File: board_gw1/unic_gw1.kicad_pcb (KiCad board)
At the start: 4 copper layers, 49.5 x 15.2 mm, 112 parts, among them Q1 2N7002, Q10 2N7002, Q11 2N7002, Q12 2N7002, Q13 2N7002, Q14 2N7002, Q15 2N7002, Q16 2N7002, Q17 2N7002, Q18 2N7002, Q19 2N7002, Q2 2N7002, Q20 2N7002, Q21 2N7002, Q22 2N7002, Q23 2N7002, Q24 2N7002, Q25 2N7002, Q26 2N7002, Q27 2N7002, Q28 2N7002, Q29 2N7002, Q3 2N7002, Q30 2N7002, Q31 2N7002, Q32 2N7002, Q33 2N7002, Q34 2N7002, Q35 2N7002, Q36 2N7002, Q37 2N7002, Q38 2N7002, Q39 2N7002, Q4 2N7002, Q40 2N7002, Q5 2N7002, Q6 2N7002, Q7 2N7002, Q8 2N7002, Q9 2N7002, U1 GW1N-LV9QN88C6_I5_, U2 LM3480-3.3, U3 AP2202K-ADJ, U4 APS6404L-3SQR-ZR, U6 AP62150Z6, U7 W25Q16JVUXIQ, X1 27MHz

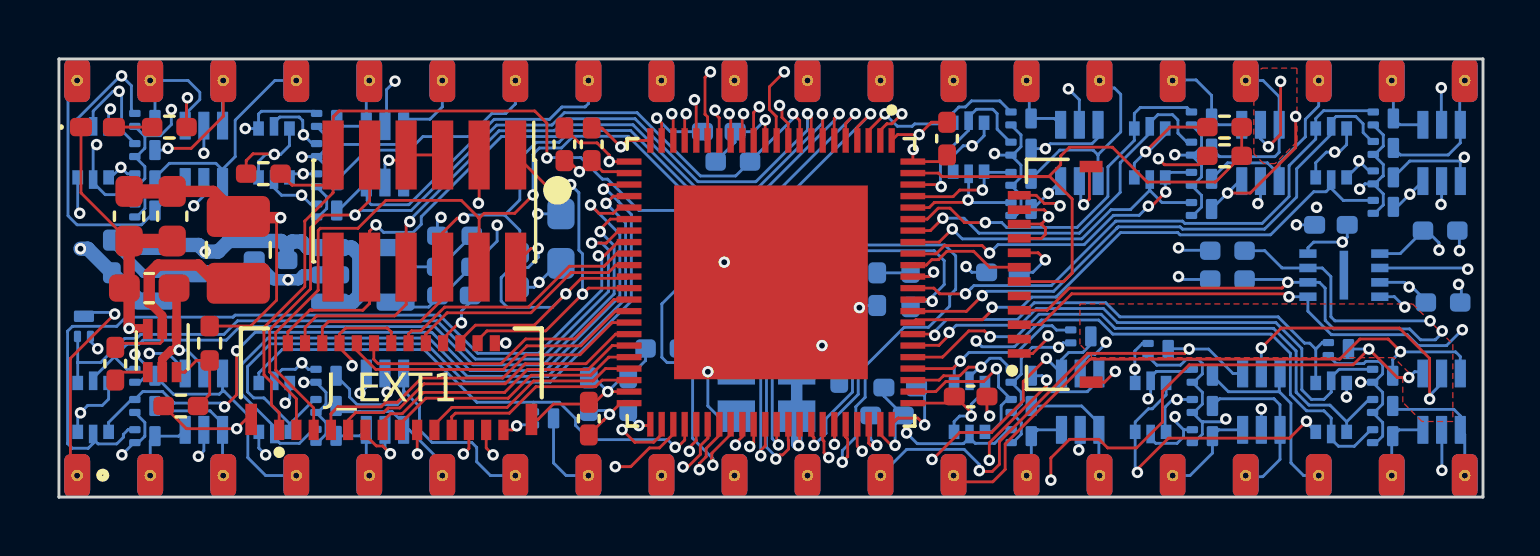
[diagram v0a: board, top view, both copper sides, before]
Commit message: Switched back to 0805 caps: they're cheaper. TODO: part number updates.
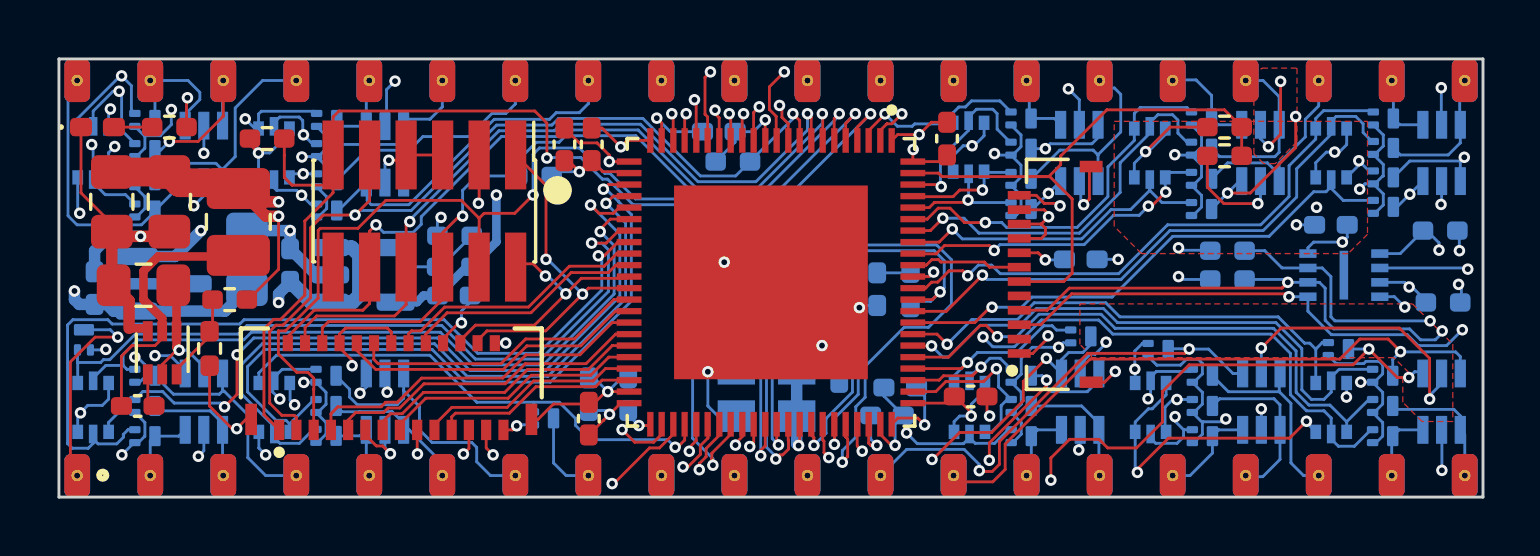
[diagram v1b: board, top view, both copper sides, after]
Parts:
- C12, C5, C7, C8: footprint Capacitor_SMD:C_0603_1608Metric_Pad1.08x0.95mm_HandSolder -> Capacitor_SMD:C_0805_2012Metric_Pad1.18x1.45mm_HandSolder
- moved C12 10.9 mm to (131.0, 94.6), turned to 90 degrees
- moved R6 3.31 mm to (141.0, 91.7), turned to 0 degrees
- moved R12 2.89 mm to (146.9, 95.2), turned to 90 degrees
- moved C16 2.74 mm to (160.0, 94.6), turned to 180 degrees
- moved R5 2.24 mm to (129.7, 97.7), turned to -90 degrees
- moved R4 1.67 mm to (130.4, 96.0), turned to 180 degrees
- moved C6 1.66 mm to (127.2, 99.7), turned to 180 degrees
- moved C2 1.25 mm to (125.7, 95.6)
- moved R16 1.23 mm to (131.7, 90.4)
- moved L1 0.97 mm to (130.7, 93.3)
- moved C7 0.78 mm to (126.3, 92.6)
- moved C1 0.70 mm to (132.5, 94.8), turned to 90 degrees
- moved U2 0.69 mm to (128.1, 95.5)
- moved C8 0.51 mm to (128.3, 92.6)
- moved Q1 0.47 mm to (125.3, 97.4)
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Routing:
- net /IO6A: track 13.0 -> 8.88 mm
- net /SPI_IO2: track 46.5 -> 44.1 mm
- net LINE: track 47.9 -> 45.9 mm, vias 12 -> 13
- net Net-(U6-SW): track 7.73 -> 9.54 mm
- net /JTAG_TCK: track 26.1 -> 24.4 mm
- net +3V3: track 73.5 -> 74.9 mm, vias 30 -> 29
- net /JTAG_SEL_N: track 37.5 -> 38.7 mm
- net /PIN1: track 10.9 -> 9.83 mm
- net +5V: track 54.5 -> 55.5 mm
- net GND: track 81.0 -> 81.8 mm, vias 39 -> 37
- net +1V2: track 40.6 -> 39.7 mm, vias 5 -> 6
- net /PIN1_F: track 25.5 -> 24.9 mm
- added copper zone on F.Cu, net +3V3

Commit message: Ready to roll with DEVEL board!
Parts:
- J_DISPLAY1: footprint UNIC:HRS_FH19C-12S-0.5SH_05_ -> UNIC:CF31121D0R0-05-NH
- moved D2 0.42 mm to (136.2, 99.5)
- moved C16 0.22 mm to (160.2, 94.7), turned to 0 degrees
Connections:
- J_DISPLAY1 pad 10: +3V3 -> /SPI_MOSI_IO0
- J_DISPLAY1 pad 11: +3V3 -> unconnected-(J_DISPLAY1-Pin_11-Pad11)
- J_DISPLAY1 pad 2: unconnected-(J_DISPLAY1-Pin_2-Pad2) -> +3V3
- J_DISPLAY1 pad 3: /SPI_MOSI_IO0 -> +3V3
- J_DISPLAY1 pad 4: /SPI_CLK -> +3V3
- J_DISPLAY1 pad 5: unconnected-(J_DISPLAY1-Pin_5-Pad5) -> GND
- J_DISPLAY1 pad 6: /LCD_RST_N -> /LCD_CS_N
- J_DISPLAY1 pad 7: /LCD_CS_N -> /LCD_RST_N
- J_DISPLAY1 pad 8: GND -> unconnected-(J_DISPLAY1-Pin_8-Pad8)
- J_DISPLAY1 pad 9: +3V3 -> /SPI_CLK
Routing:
- net /LCD_RST_N: track 20.3 -> 18.2 mm
- net /PIN8: track 13.5 -> 12.1 mm
- net +3V3: track 74.9 -> 76.2 mm, vias 29 -> 28
- net /SPI_MOSI_IO0: track 52.3 -> 53.5 mm
- net /PIN7: track 9.75 -> 8.73 mm
- net GND: track 81.8 -> 82.5 mm, vias 37 -> 38
- net LINE: track 45.9 -> 46.4 mm
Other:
- board text added: "Standard DIP40 top"

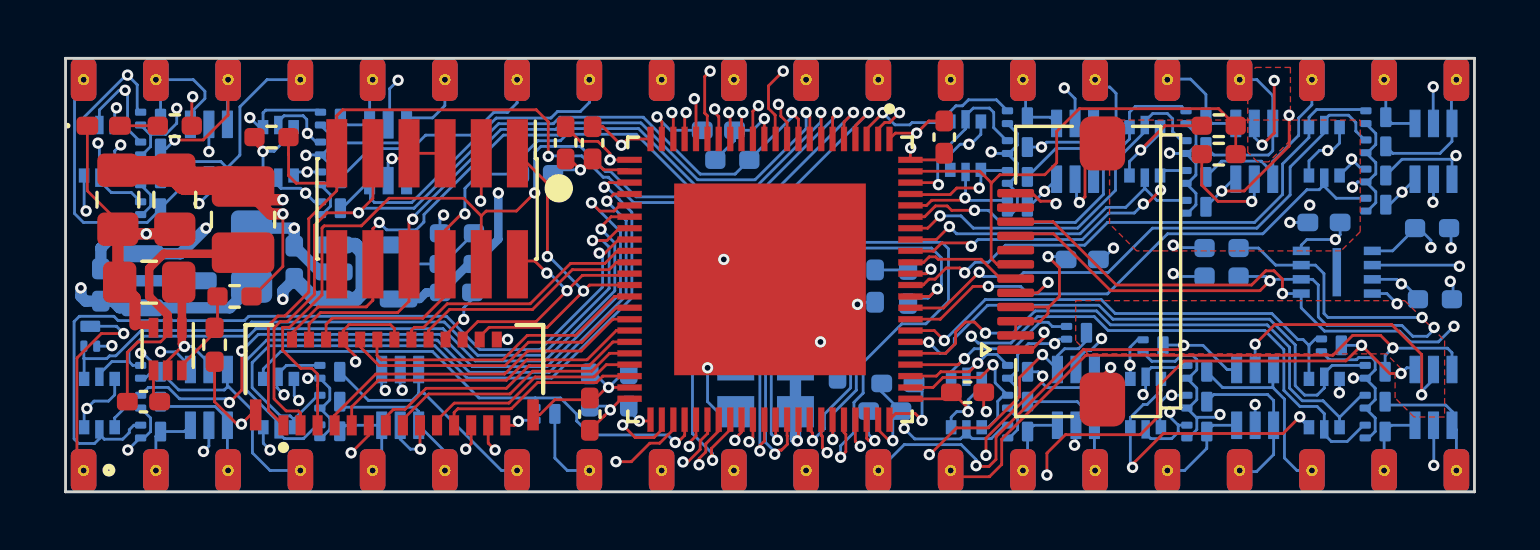
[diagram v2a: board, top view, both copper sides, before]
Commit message: Updated board file; started cover CAD.
This checkin marks the hopefully complete V1.0 design for the form-factor
board.

It also contains the first (incomplete) iteration of the cover design.
It has a bunch of interference with components on the PCB which
needs to be cleaned. It's also unclear if snaps have to be 1.5mm thick.
Seems excessive. Finally, I don't think the OLED display can even survive
such stiff snaps. But it at least a start.
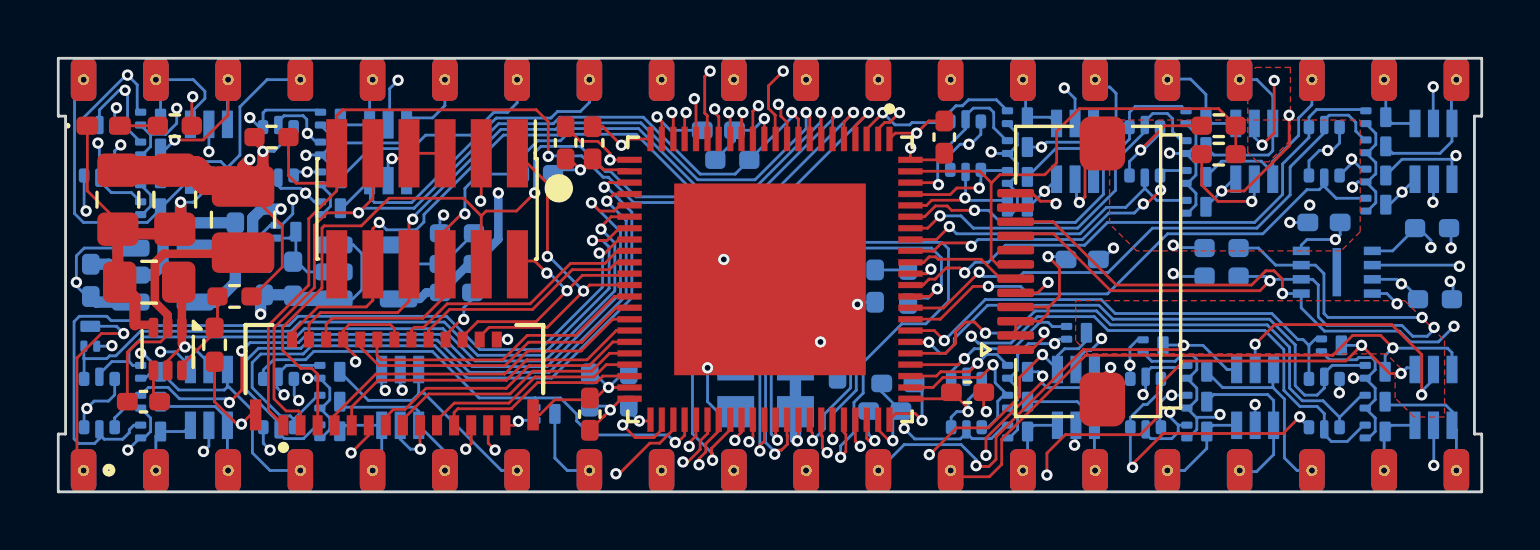
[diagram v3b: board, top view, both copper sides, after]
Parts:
- removed C12: 10u, Capacitor_SMD:C_0805_2012Metric_Pad1.18x1.45mm_HandSolder
- removed U2: LM3480-3.3, Package_TO_SOT_SMD:SOT-23
- added C10: 2.2u, Capacitor_SMD:C_0402_1005Metric_Pad0.74x0.62mm_HandSolder, B.Cu at (125.3, 95.4)
- added Q41: 2N7002, UNIC:SOT-883, B.Cu at (132.2, 93.7)
- added R17: 100k, Resistor_SMD:R_0402_1005Metric_Pad0.72x0.64mm_HandSolder, B.Cu at (132.5, 95.4)
- added U5: MIC5504-1.2YM5, Package_TO_SOT_SMD:SOT-23-5, B.Cu at (127.9, 95.2)
- R4: value 4.99k -> 31.6k
- U3: value AP2202K-ADJ -> MIC5203-3.3BM5
- moved C2 5.00 mm to (130.4, 94.0)
- moved C1 1.20 mm to (131.4, 95.4)
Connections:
- C2 pad 1: +3V3 -> +1V2
- C7 pad 1: +1V2 -> +3V3
- C8 pad 1: +1V2 -> +3V3
- L1 pad 2: +1V2 -> +3V3
- R4 pad 1: +1V2 -> +3V3
- U3 pad 2: GND -> Net-(Q41-D)
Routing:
- net +3V3: track 76.2 -> 86.2 mm, vias 28 -> 29
- net +1V2: track 39.7 -> 34.6 mm, vias 6 -> 5
- net Net-(Q41-D): track 0.00 -> 3.31 mm
- net LINE: track 46.4 -> 44.2 mm, vias 13 -> 12
- net /LCD_CS_N: track 4.10 -> 3.56 mm
- net GND: track 82.5 -> 82.2 mm, vias 38 -> 37
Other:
- board size 49.5 x 15.2 mm -> 50 x 15.2 mm

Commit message: Added test-points, edge clearance, some cleanup.
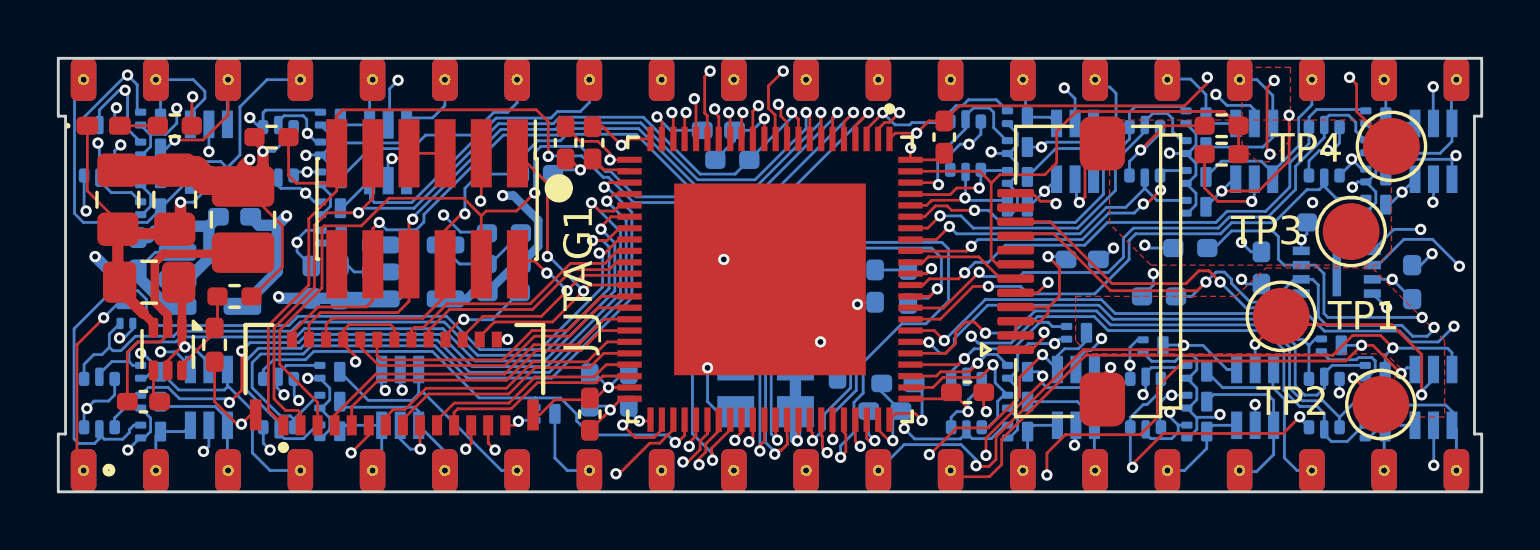
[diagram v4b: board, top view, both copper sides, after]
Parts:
- added TP1: TestPoint, TestPoint:TestPoint_Pad_D2.0mm, F.Cu at (167.2, 96.7)
- added TP2: TestPoint, TestPoint:TestPoint_Pad_D2.0mm, F.Cu at (170.7, 99.8)
- added TP3: TestPoint, TestPoint:TestPoint_Pad_D2.0mm, F.Cu at (169.7, 93.7)
- added TP4: TestPoint, TestPoint:TestPoint_Pad_D2.0mm, F.Cu at (171.1, 90.7)
- moved R8 3.81 mm to (168.7, 93.4), turned to 0 degrees
- moved C14 2.72 mm to (166.5, 95.0), turned to -90 degrees
- moved R11 2.31 mm to (162.9, 96.0)
- moved C10 1.90 mm to (127.0, 94.5)
- moved C1 1.66 mm to (133.1, 95.5)
- moved U5 1.66 mm to (129.5, 95.4)
- moved C3 1.65 mm to (139.9, 95.9)
- moved R15 1.65 mm to (139.9, 93.8)
- moved U3 1.65 mm to (136.7, 95.1)
- moved R14 1.65 mm to (139.9, 94.9)
- moved R17 1.64 mm to (134.1, 95.5)
- moved Q41 1.60 mm to (133.8, 93.9)
- moved Q1 1.50 mm to (126.6, 96.6)
- moved R10 1.10 mm to (164.0, 94.3)
- moved R9 1.00 mm to (171.8, 95.5), turned to -90 degrees
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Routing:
- net +1V2: track 34.6 -> 52.5 mm, vias 5 -> 7
- net +5V: track 55.3 -> 57.5 mm
- net LINE: track 44.2 -> 46.1 mm, vias 12 -> 13
- net /SPI_IO3: track 44.3 -> 46.1 mm
- net /FLASH_CS_N: track 35.2 -> 36.4 mm
- net /PIN2_F: track 30.1 -> 31.0 mm
- net /SPI_CLK: track 53.6 -> 54.4 mm
- net +3V3: track 86.2 -> 85.4 mm
- net /PIN29: track 20.4 -> 21.2 mm
- net GND: track 82.2 -> 81.5 mm
- net /PIN1_F: track 24.9 -> 25.4 mm

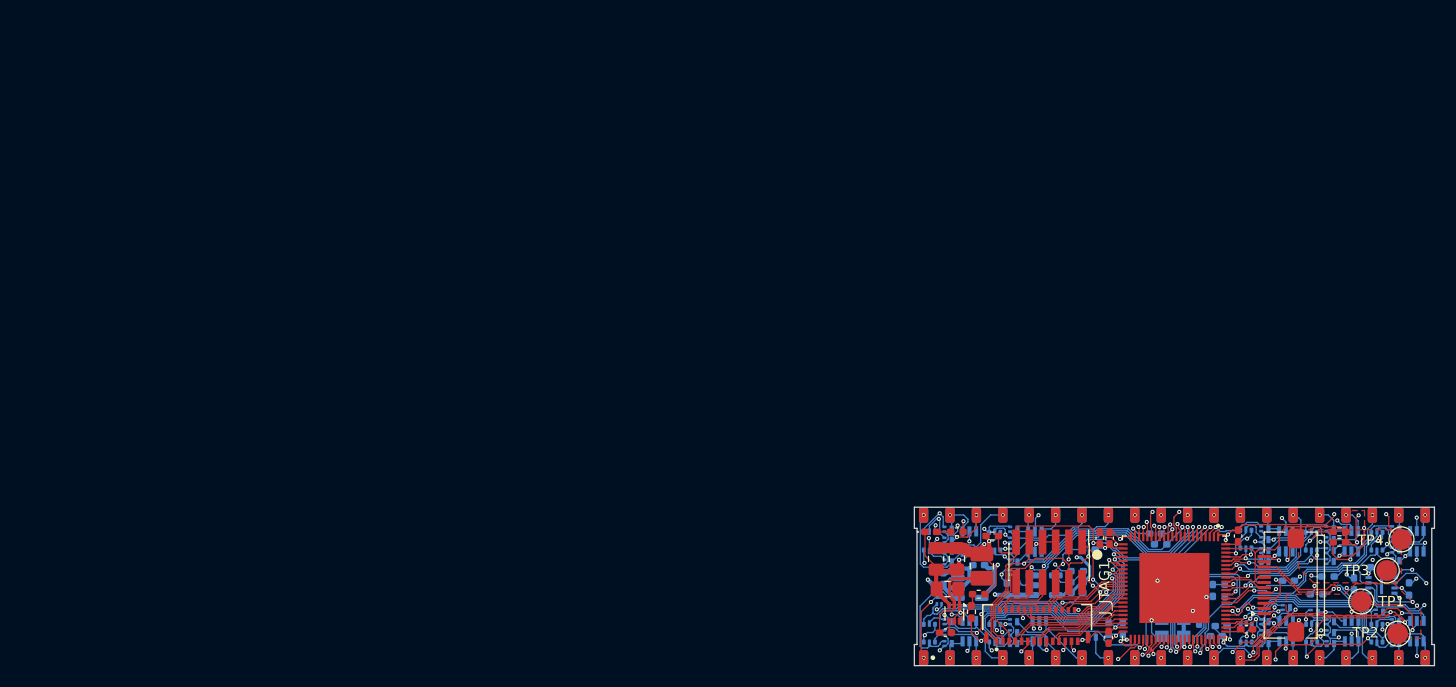
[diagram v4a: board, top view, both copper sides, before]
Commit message: Added fiducials and some other flourishes.
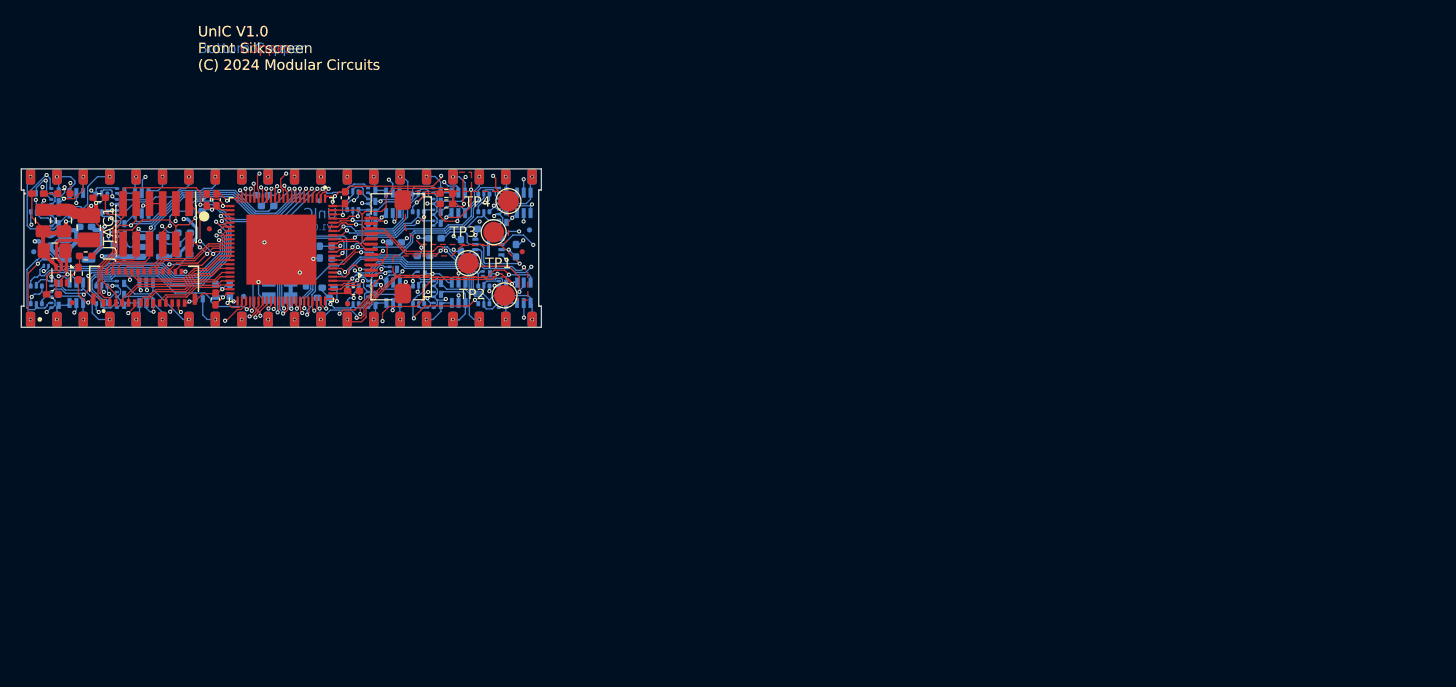
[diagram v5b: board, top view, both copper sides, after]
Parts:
- added FID1: Fiducial, Fiducial:Fiducial_0.5mm_Mask1mm, B.Cu at (67.0, 58.1)
- added FID2: Fiducial, Fiducial:Fiducial_0.5mm_Mask1mm, F.Cu at (70.9, 57.4)
- added FID3: Fiducial, Fiducial:Fiducial_0.5mm_Mask1mm, B.Cu at (87.2, 61.0)
- added FID4: Fiducial, Fiducial:Fiducial_0.5mm_Mask1mm, F.Cu at (43.2, 68.0)
- added FID5: Fiducial, Fiducial:Fiducial_0.5mm_Mask1mm, B.Cu at (39.5, 63.0)
- added FID6: Fiducial, Fiducial:Fiducial_0.5mm_Mask1mm, F.Cu at (86.5, 63.0)
- added FID7: Fiducial, Fiducial:Fiducial_0.5mm_Mask1mm, B.Cu at (59.7, 67.3)
- added FID8: Fiducial, Fiducial:Fiducial_0.5mm_Mask1mm, F.Cu at (56.4, 60.9)
- added FID9: Fiducial, Fiducial:Fiducial_0.5mm_Mask1mm, F.Cu at (69.7, 68.0)
- moved C2 91.9 mm to (44.5, 60.6)
- moved C20 91.9 mm to (57.1, 58.0)
- moved C5 91.9 mm to (41.5, 63.0)
- moved C8 91.9 mm to (42.4, 60.0)
- moved D11 91.9 mm to (86.6, 58.4)
- moved D21 91.9 mm to (39.7, 67.2)
- moved D24 91.9 mm to (76.5, 67.2)
- moved D25 91.9 mm to (82.8, 67.2)
- moved D26 91.9 mm to (82.8, 58.4)
- moved D30 91.9 mm to (39.7, 58.4)
- moved D5 91.9 mm to (86.6, 67.0)
- moved D8 91.9 mm to (49.9, 58.4)
- moved J_EXT1 91.9 mm to (50.1, 66.4)
- moved Q10 91.9 mm to (72.0, 66.1)
- moved Q11 91.9 mm to (84.6, 57.1)
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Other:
- board text added: "(C) 2024 MC"
- board text added: "A"
- board text added: "K"
- board text added: "UnIC"
- board text added: "UnIC V1.0 Bottom Copper (C) 2024 Modular Circuits"
- board text added: "UnIC V1.0 Bottom Fab Drawing (C) 2024 Modular Circuits"
- board text added: "UnIC V1.0 Bottom Mask (C) 2024 Modular Circuits"
- board text added: "UnIC V1.0 Bottom Paste (C) 2024 Modular Circuits"
- board text added: "UnIC V1.0 Front Copper (C) 2024 Modular Circuits"
- board text added: "UnIC V1.0 Front Fab Drawing (C) 2024 Modular Circuits"
- board text added: "UnIC V1.0 Front Mask (C) 2024 Modular Circuits"
- board text added: "UnIC V1.0 Front Paste (C) 2024 Modular Circuits"
- board text added: "UnIC V1.0 Front Silkscreen (C) 2024 Modular Circuits"
- board text added: "UnIC V1.0 Layer 2 Copper (C) 2024 Modular Circuits"
- board text added: "UnIC V1.0 Layer 3 Copper (C) 2024 Modular Circuits"
- board text added: "V1.0"
